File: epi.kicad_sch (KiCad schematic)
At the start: 31 parts, among them J1 Connector 1x12, J2 Connector 1x12, J3 Conn_01x05, J4 USB-C 2.0 mid-mount female co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, U1 ATmega32U4-M, Y1 Crystal_GND24

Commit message: new computer, new updates
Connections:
- net A5: now also J3.5 (Pin_5); no longer J3.4 (Pin_4)
- net GND: no longer J3.5 (Pin_5)
- net D17/SS: now reaches U1.8 (PB0)
- net D17/SS: now also J3.4 (Pin_4)
- no-connect marks 6 -> 5

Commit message: messing with outline and also spark gap
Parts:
- added E1: SparkGap, DIY:sparkgap_epi, symbol Device:SparkGap
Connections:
- net GND: now also E1.2
- net at FB1.1, J4.A4 (VBUS), J4.A9 (VBUS)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: now also E1.1
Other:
- moved on the sheet: D2, F1, FB1, RV3

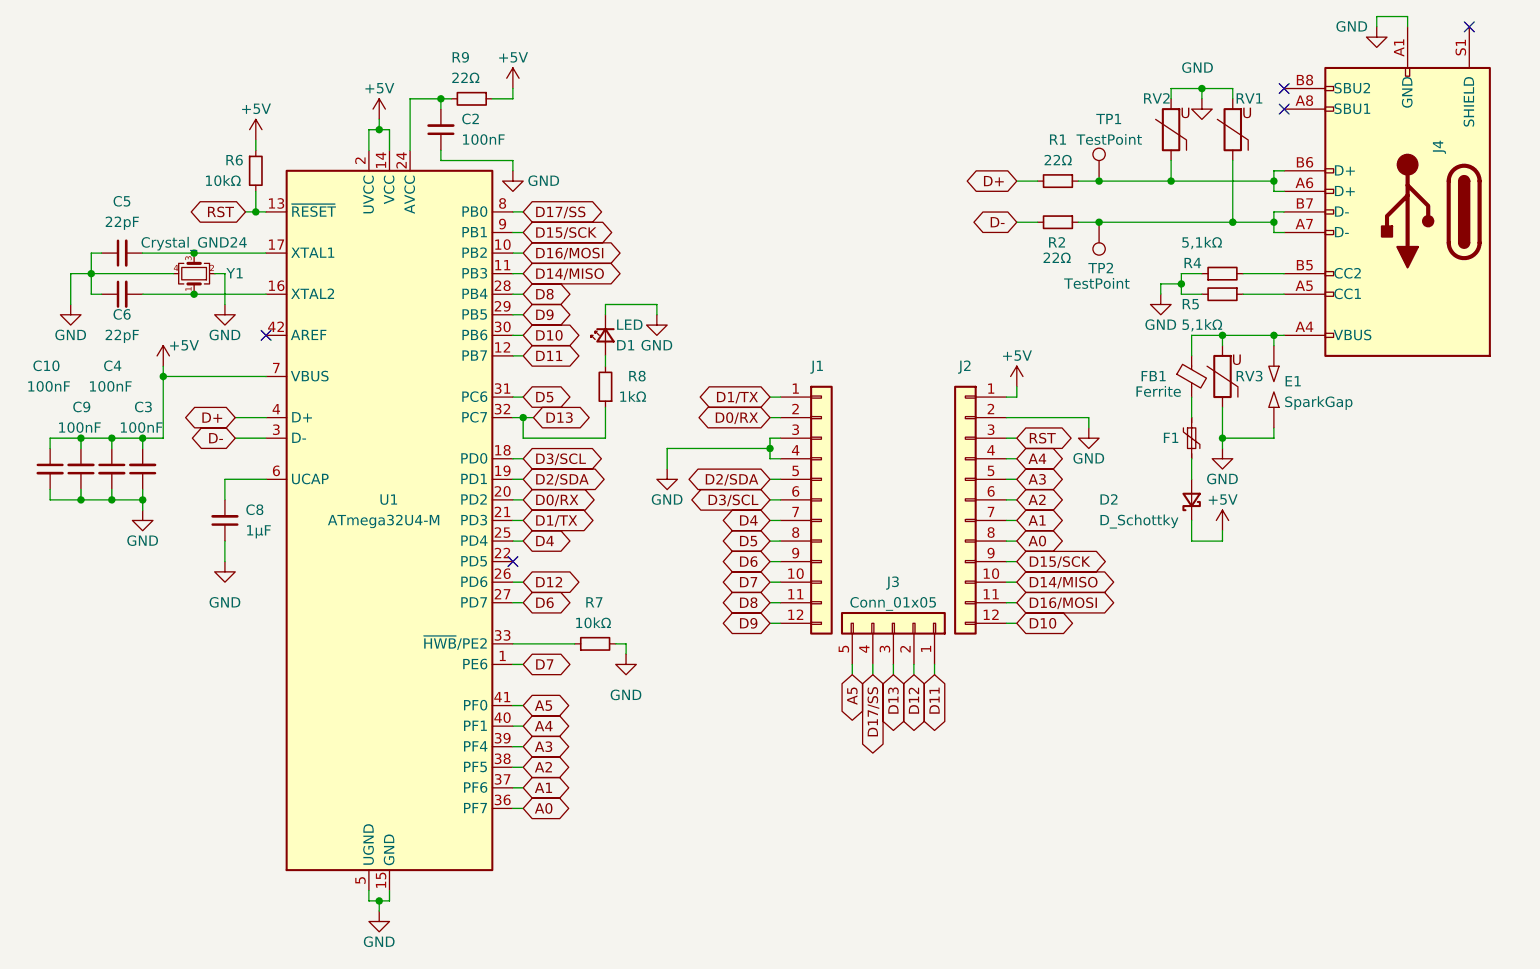
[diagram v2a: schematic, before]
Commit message: USB shield connection set up
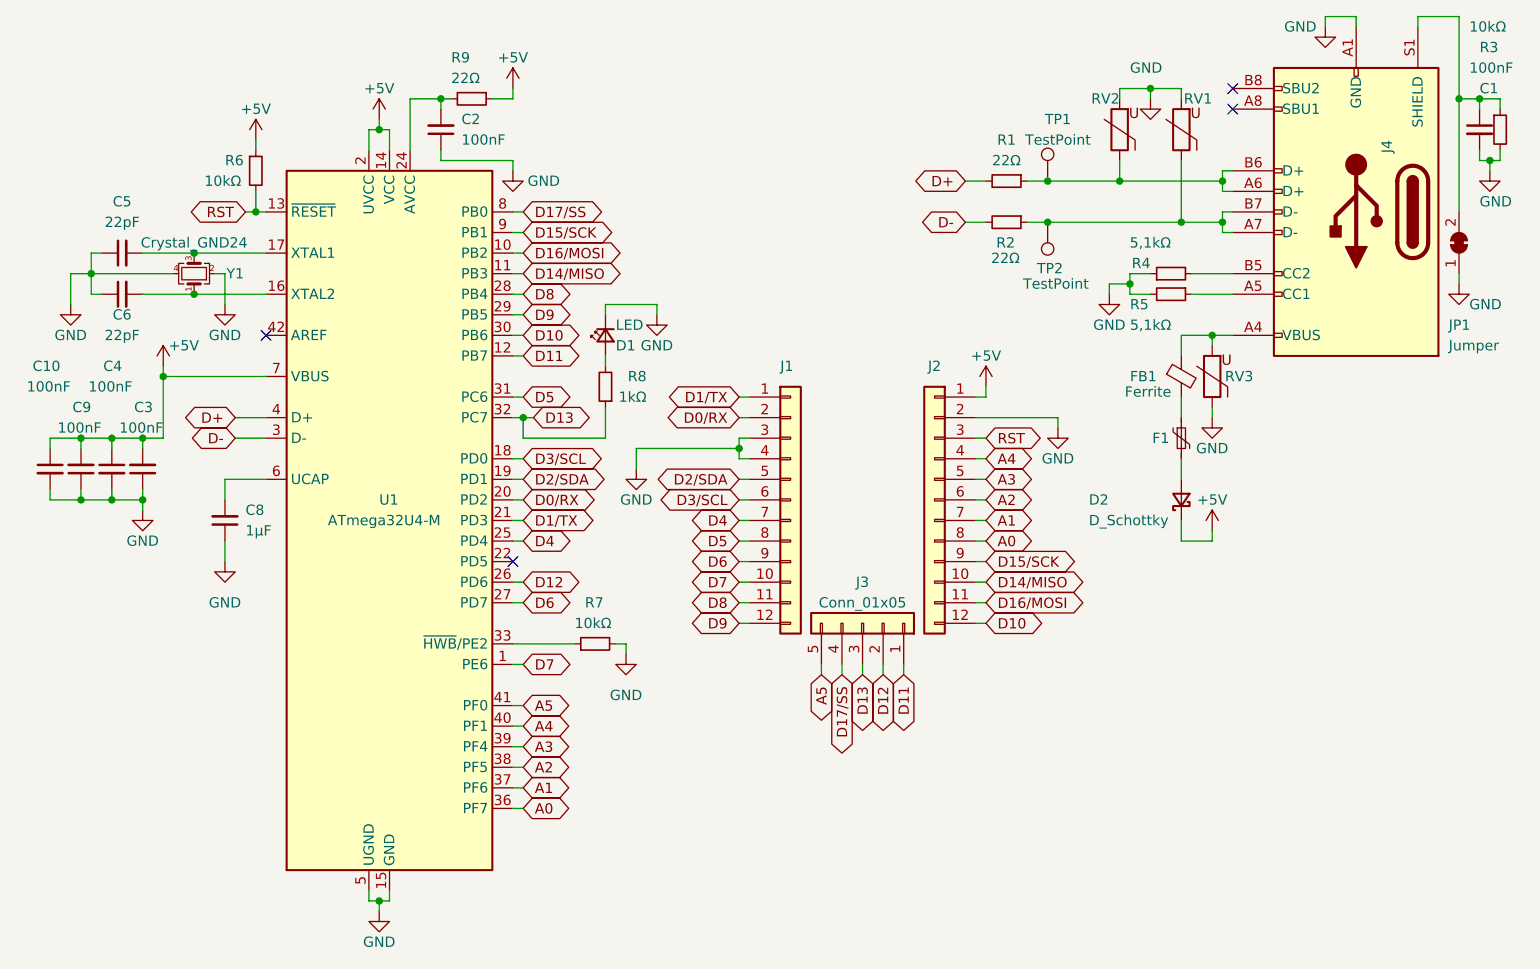
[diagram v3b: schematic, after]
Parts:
- removed E1: SparkGap, DIY:sparkgap_epi, symbol Device:SparkGap
- added C1: 100nF, Capacitor_SMD:C_0402_1005Metric, symbol Device:C_Small
- added JP1: Jumper, Jumper:SolderJumper-2_P1.3mm_Bridged_RoundedPad1.0x1.5mm, symbol Jumper:SolderJumper_2_Bridged
- added R3: 10kΩ, Resistor_SMD:R_0402_1005Metric, symbol Device:R_Small
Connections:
- net GND: now also C1.2, JP1.1 (A), R3.2
- net at J4.S1 (SHIELD): now also C1.1, JP1.2 (B), R3.1
- no-connect marks 5 -> 4
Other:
- moved on the sheet: D2, F1, FB1, J1, J2, J3, J4, R1, R2, R4, R5, RV1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

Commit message: big redesign
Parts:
- added C7: 10µF, Resistor_SMD:R_0402_1005Metric, symbol Device:C_Small
- C1, C10, C2, C3, C4, C5, C6, C8, C9: footprint Capacitor_SMD:C_0402_1005Metric -> Resistor_SMD:R_0402_1005Metric
- F1: footprint Fuse:Fuse_0402_1005Metric -> Resistor_SMD:R_0402_1005Metric
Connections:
- net D13: now also D1.2 (A); no longer R8.1
- net GND: now also R8.2, C7.2; no longer D1.1 (K)
- net at F1.1, FB1.2: now also C7.1
- new net: D1.1 (K), R8.1
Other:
- moved on the sheet: D1, R8
